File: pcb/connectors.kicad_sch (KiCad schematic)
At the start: 5 parts, among them J1 GPIO, J2 Hirose_FH12-16S, J3 TC2030

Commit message: saved libraries to project
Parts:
- J1: symbol Connector_Generic:Conn_02x20_Odd_Even -> library:Conn_02x20_Odd_Even
- J2: symbol Connector_Generic:Conn_01x17 -> library:Conn_01x17
- J3: symbol Connector:TC2030 -> library:TC2030
- R24, R25: symbol Device:R_US -> library:R_US
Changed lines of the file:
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@@
 	)
 	(symbol
-		(lib_id "power:GND")
+		(lib_id "library:GND")
 		(at 100.33 124.46 0)
 		(unit 1)
@@
 	)
 	(symbol
-		(lib_id "power:GND")
+		(lib_id "library:GND")
 		(at 82.55 124.46 0)
 		(unit 1)
@@
 	)
 	(symbol
-		(lib_id "Connector_Generic:Conn_02x20_Odd_Even")
+		(lib_id "library:Conn_02x20_Odd_Even")
 		(at 90.17 95.25 0)
 		(unit 1)
@@
 	)
 	(symbol
-		(lib_id "power:GND")
+		(lib_id "library:GND")
 		(at 199.39 151.13 0)
 		(mirror y)
@@
 	)
 	(symbol
-		(lib_id "Device:R_US")
+		(lib_id "library:R_US")
 		(at 238.76 127 0)
 		(unit 1)
@@
 	)
 	(symbol
-		(lib_id "Connector_Generic:Conn_01x17")
+		(lib_id "library:Conn_01x17")
 		(at 191.77 121.92 0)
 		(mirror y)
@@
 	)
 	(symbol
-		(lib_id "Device:R_US")
+		(lib_id "library:R_US")
 		(at 227.33 144.78 0)
 		(unit 1)
@@
 	)
 	(symbol
-		(lib_id "power:GND")
+		(lib_id "library:GND")
 		(at 227.33 151.13 0)
 		(mirror y)
@@
 	)
 	(symbol
-		(lib_id "Connector:TC2030")
+		(lib_id "library:TC2030")
 		(at 218.44 60.96 0)
 		(unit 1)
@@
 	)
 	(symbol
-		(lib_id "power:GND")
+		(lib_id "library:GND")
 		(at 205.74 63.5 0)
 		(unit 1)

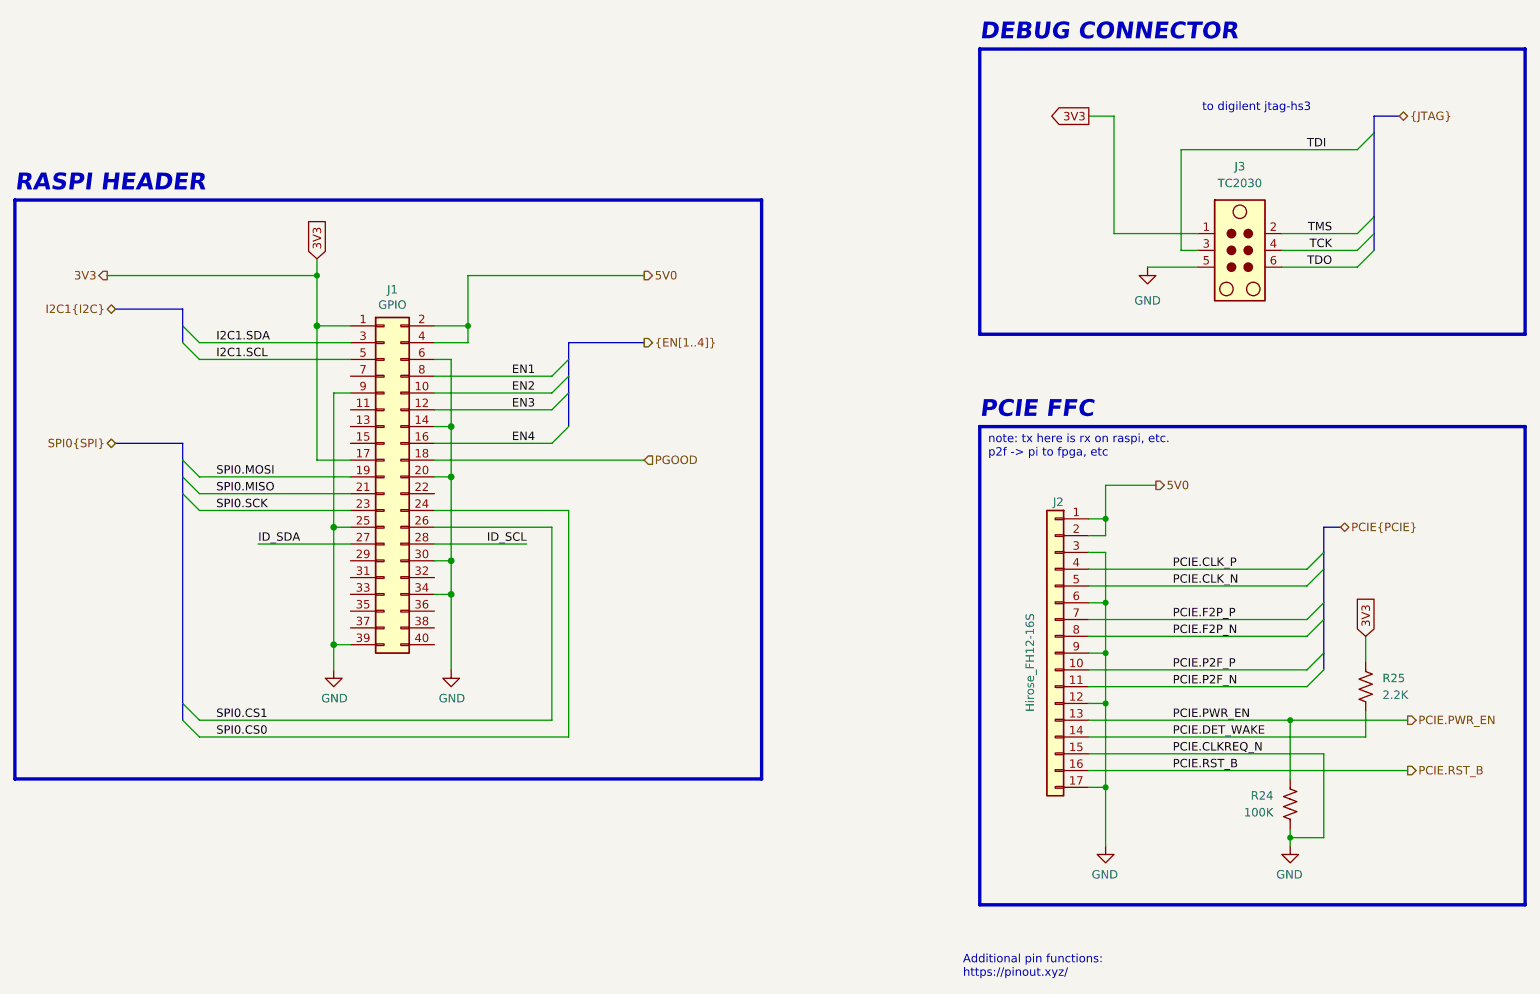
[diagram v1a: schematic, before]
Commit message: hierarchy and power sequencing, level shift
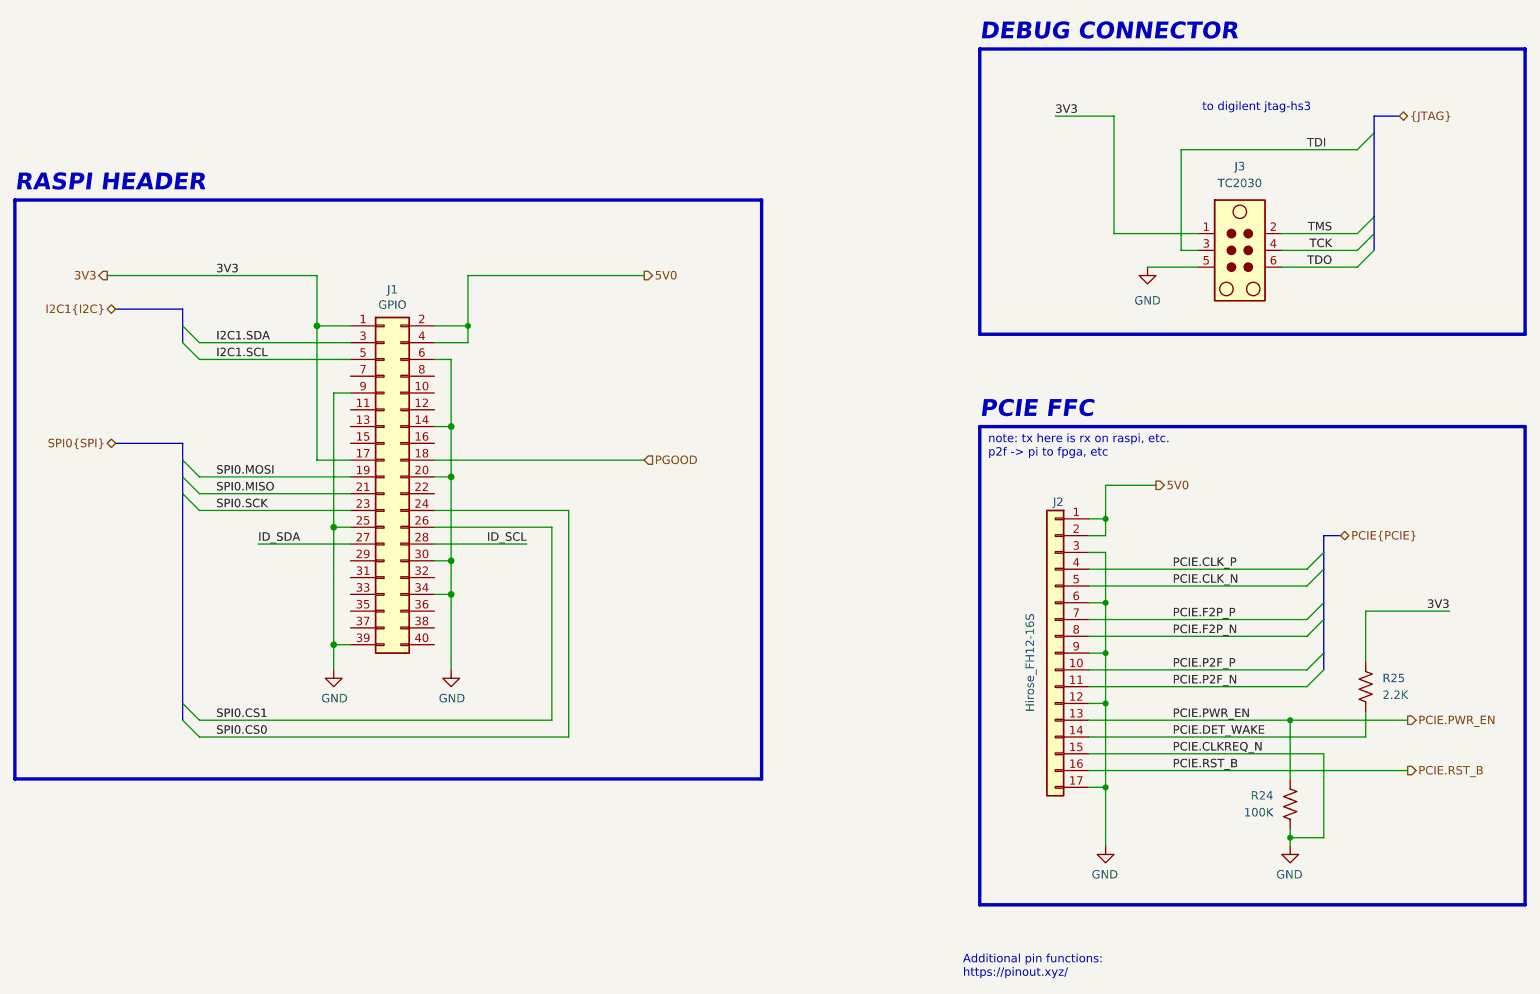
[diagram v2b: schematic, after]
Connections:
- net EN1: no longer names the net of J1.8 (Pin_8)
- net EN2: no longer names the net of J1.10 (Pin_10)
- net EN3: no longer names the net of J1.12 (Pin_12)
- net EN4: no longer names the net of J1.16 (Pin_16)

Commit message: defined memory pinouts
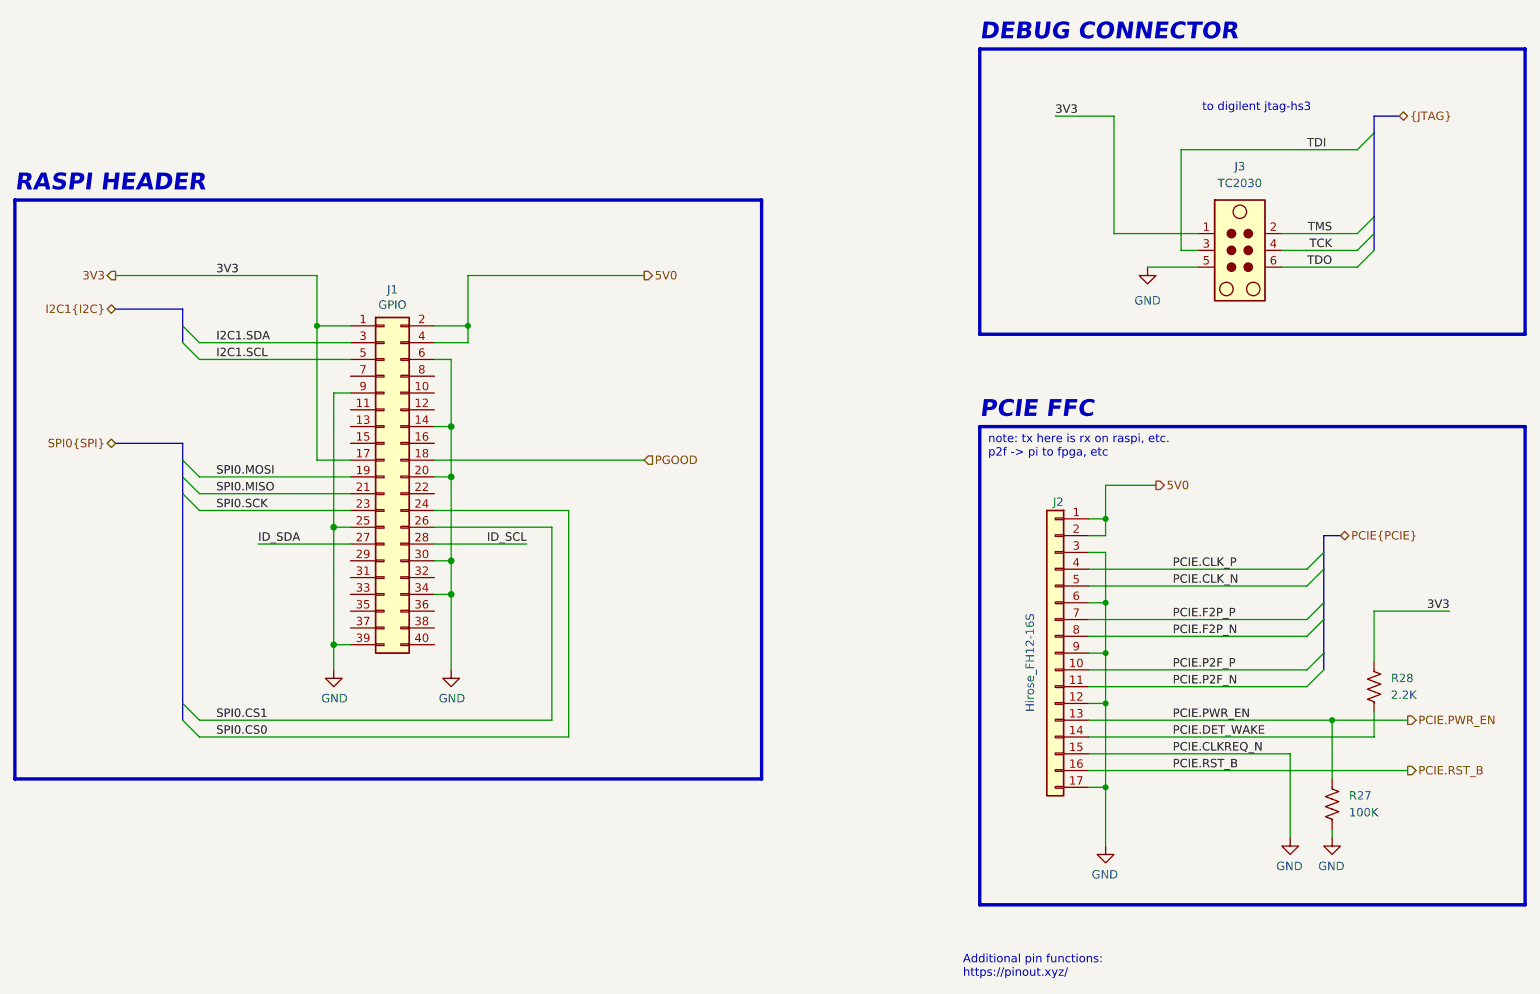
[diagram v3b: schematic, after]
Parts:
- renumbered R24 to R27, R25 to R28
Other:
- moved on the sheet: R27, R28

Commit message: power restructuring
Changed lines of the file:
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@@
-		)
-	)
-	(wire
-		(pts
-			(xy 226.06 58.42) (xy 237.49 58.42)
-		)
-		(stroke
-			(width 0)
-			(type default)
 		)
 	)
@@
 	(wire
 		(pts
-			(xy 237.49 45.72) (xy 210.82 45.72)
+			(xy 237.49 45.72) (xy 208.28 45.72)
+		)
+		(stroke
+			(width 0)
+			(type default)
+		)
+	)
+	(wire
+		(pts
+			(xy 228.6 60.96) (xy 237.49 60.96)
 		)
 		(stroke
@@
 	(wire
 		(pts
-			(xy 226.06 60.96) (xy 237.49 60.96)
-		)
-		(stroke
-			(width 0)
-			(type default)
-		)
-	)
-	(wire
-		(pts
 			(xy 196.85 116.84) (xy 229.87 116.84)
 		)
@@
 	(wire
 		(pts
+			(xy 209.55 63.5) (xy 209.55 64.77)
+		)
+		(stroke
+			(width 0)
+			(type default)
+		)
+	)
+	(wire
+		(pts
 			(xy 100.33 95.25) (xy 100.33 107.95)
 		)
@@
 	(wire
 		(pts
-			(xy 210.82 45.72) (xy 210.82 60.96)
+			(xy 208.28 45.72) (xy 208.28 60.96)
+		)
+		(stroke
+			(width 0)
+			(type default)
+		)
+	)
+	(wire
+		(pts
+			(xy 228.6 63.5) (xy 237.49 63.5)
 		)
 		(stroke
@@
 	(wire
 		(pts
-			(xy 226.06 63.5) (xy 237.49 63.5)
+			(xy 209.55 63.5) (xy 210.82 63.5)
 		)
 		(stroke
@@
 	(wire
 		(pts
-			(xy 210.82 60.96) (xy 213.36 60.96)
-		)
-		(stroke
-			(width 0)
-			(type default)
-		)
-	)
-	(wire
-		(pts
 			(xy 100.33 113.03) (xy 100.33 124.46)
 		)
@@
 	(wire
 		(pts
+			(xy 208.28 60.96) (xy 210.82 60.96)
+		)
+		(stroke
+			(width 0)
+			(type default)
+		)
+	)
+	(wire
+		(pts
 			(xy 80.01 72.39) (xy 80.01 92.71)
 		)
@@
 	(wire
 		(pts
-			(xy 205.74 63.5) (xy 213.36 63.5)
-		)
-		(stroke
-			(width 0)
-			(type default)
-		)
-	)
-	(wire
-		(pts
 			(xy 196.85 124.46) (xy 229.87 124.46)
 		)
@@
 	(wire
 		(pts
+			(xy 200.66 58.42) (xy 210.82 58.42)
+		)
+		(stroke
+			(width 0.254)
+			(type default)
+			(color 0 0 255 1)
+		)
+	)
+	(wire
+		(pts
 			(xy 199.39 104.14) (xy 199.39 101.6)
 		)
@@
 		)
 	)
+	(wire
+		(pts
+			(xy 228.6 58.42) (xy 237.49 58.42)
+		)
+		(stroke
+			(width 0)
+			(type default)
+		)
+	)
 	(bus
 		(pts
@@
 			(width 0)
 			(type solid)
-		)
-	)
-	(wire
-		(pts
-			(xy 200.66 58.42) (xy 213.36 58.42)
-		)
-		(stroke
-			(width 0.254)
-			(type default)
-			(color 0 0 255 1)
 		)
 	)
@@
 			)
 		)
+		(property "Name" ""
+			(at 218.44 60.96 0)
+			(effects
+				(font
+					(size 1.27 1.27)
+				)
+				(hide yes)
+			)
+		)
 		(pin "3"
 		)
@@
 	(symbol
 		(lib_id "library:GND")
-		(at 205.74 63.5 0)
+		(at 209.55 64.77 0)
 		(unit 1)
 		(exclude_from_sim no)
@@
 		(fields_autoplaced yes)
 		(property "Reference" "#PWR034"
-			(at 205.74 69.85 0)
+			(at 209.55 71.12 0)
 			(effects
 				(font
@@
 		)
 		(property "Value" "GND"
-			(at 205.74 68.58 0)
+			(at 209.55 69.85 0)
 			(effects
 				(font
@@
 		)
 		(property "Footprint" ""
-			(at 205.74 63.5 0)
+			(at 209.55 64.77 0)
 			(effects
 				(font
@@
 		)
 		(property "Datasheet" ""
-			(at 205.74 63.5 0)
+			(at 209.55 64.77 0)
 			(effects
 				(font
@@
 		)
 		(property "Description" "Power symbol creates a global label with name \"GND\" , ground"
-			(at 205.74 63.5 0)
-			(effects
-				(font
+			(at 209.55 64.77 0)
+			(effects
+				(font

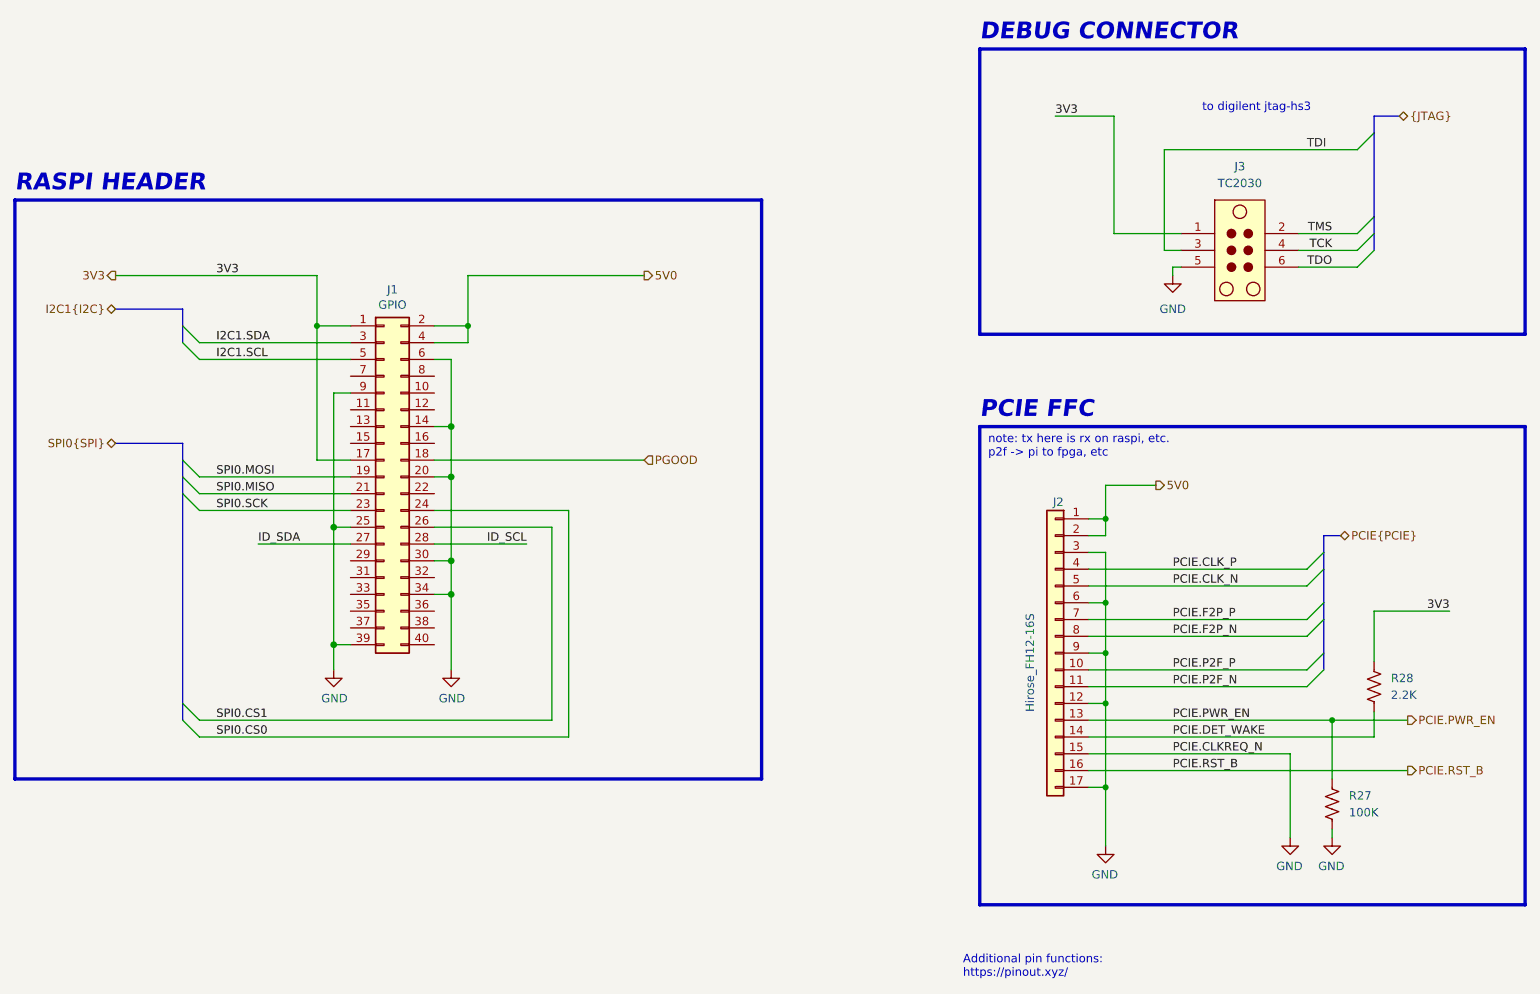
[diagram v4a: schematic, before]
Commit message: moved stuff around, bom
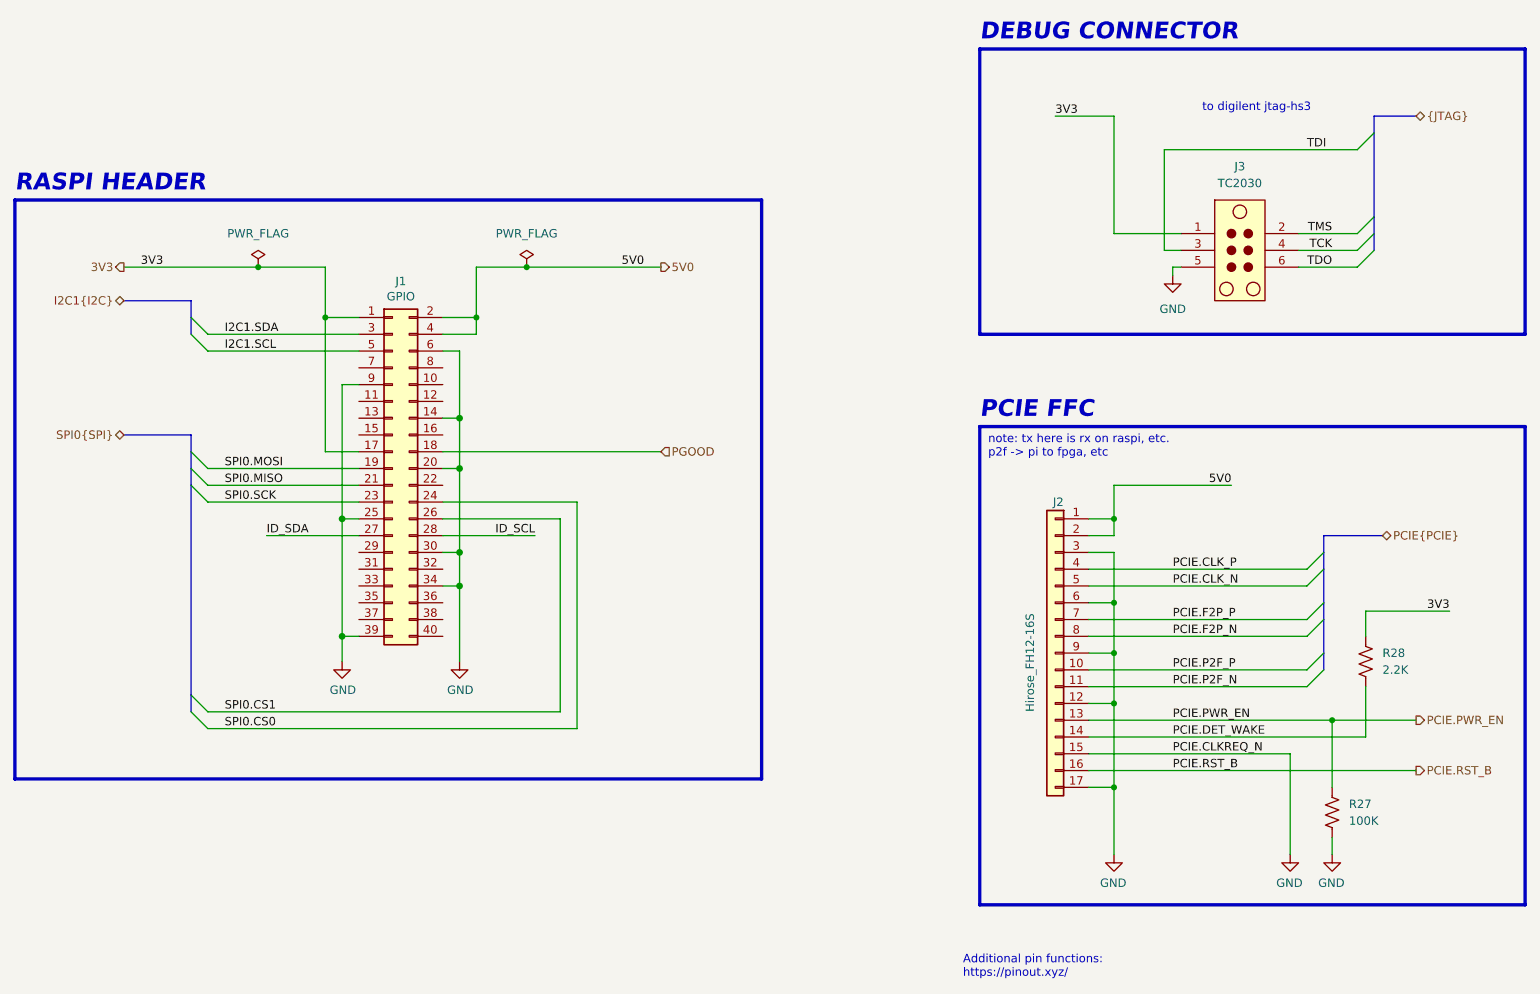
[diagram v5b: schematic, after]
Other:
- moved on the sheet: J1, R27, R28

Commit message: jtag, dcplng
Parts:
- R27: footprint Resistor_SMD:R_0402_1005Metric -> library:R_0402_1005Metric; Manufacturer (none) -> YAGEO; Manufacturer Product Number (none) -> RC0402FR-07100KL
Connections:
- net GND: now also R27.1; no longer R27.2
- net PCIE.PWR_EN: now also R27.2; no longer R27.1
- net TCK: now also J1.33 (Pin_33)
- net TDI: now also J1.37 (Pin_37)
- net TDO: now also J1.36 (Pin_36)
- net TMS: now also J1.35 (Pin_35)
- net PROG_B: now reaches J1.38 (Pin_38)
- net DONE: now reaches J1.40 (Pin_40)
- net PGOOD renamed FPGA_PG

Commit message: qspi
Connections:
- net SPI0.CS0 renamed QSPI0.CS0n
- net SPI0.CS1 renamed QSPI0.CS1n
- net SPI0.MISO renamed QSPI0.SIO1
- net SPI0.MOSI renamed QSPI0.SIO0
- net SPI0.SCK renamed QSPI0.SCLK
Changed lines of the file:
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@@
 		)
 	)
-	(label "SPI0.MISO"
+	(label "QSPI0.SIO1"
 		(at 66.04 96.52 0)
 		(effects
@@
 		)
 	)
-	(label "SPI0.CS0"
+	(label "QSPI0.CS0n"
 		(at 66.04 133.35 0)
 		(effects
@@
 		)
 	)
-	(label "SPI0.CS1"
+	(label "QSPI0.CS1n"
 		(at 66.04 130.81 0)
 		(effects
@@
 		)
 	)
-	(label "SPI0.SCK"
+	(label "QSPI0.SCLK"
 		(at 66.04 99.06 0)
 		(effects
@@
 		)
 	)
-	(label "SPI0.MOSI"
+	(label "QSPI0.SIO0"
 		(at 66.04 93.98 0)
 		(effects
@@
 		)
 	)
-	(hierarchical_label "SPI0{SPI}"
+	(hierarchical_label "QSPI0{QSPI}"
 		(shape bidirectional)
 		(at 50.8 88.9 180)
